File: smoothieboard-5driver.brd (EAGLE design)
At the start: 129.5 x 105.1 mm, 270 parts, among them IC1 LPC1769, IC10 LM1117-3.3V, IC11 78L12F, IC12 A4982, IC2 A4982, IC3 A4982, IC4 MCP44X1, IC5 A4982, IC6 A4982, IC9 MCP44X1, J10 POWER_JACKSMD, Q1 BSL207SP, Q2 12MHz, Q3 25MHz, Q4 ZXMN4A06, Q5 AOT240L, Q6 AOT240L, Q7 AOT240L, Q8 ZXMN4A06, Q9 ZXMN4A06, U1 USD-SOCKETNEW, X14 USBPTH

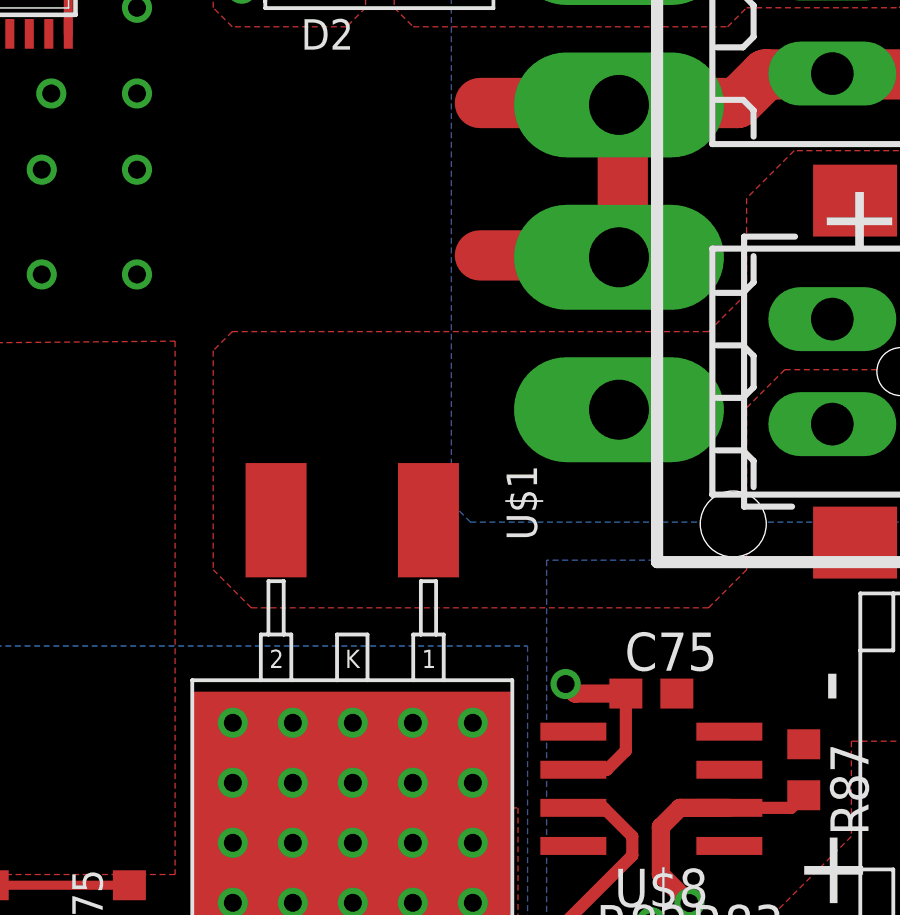
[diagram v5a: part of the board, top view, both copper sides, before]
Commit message: Change type of primary diode to a more robust type with lower Vf, add a helper diode to prevent damage from primary diode's higher reverse leakage
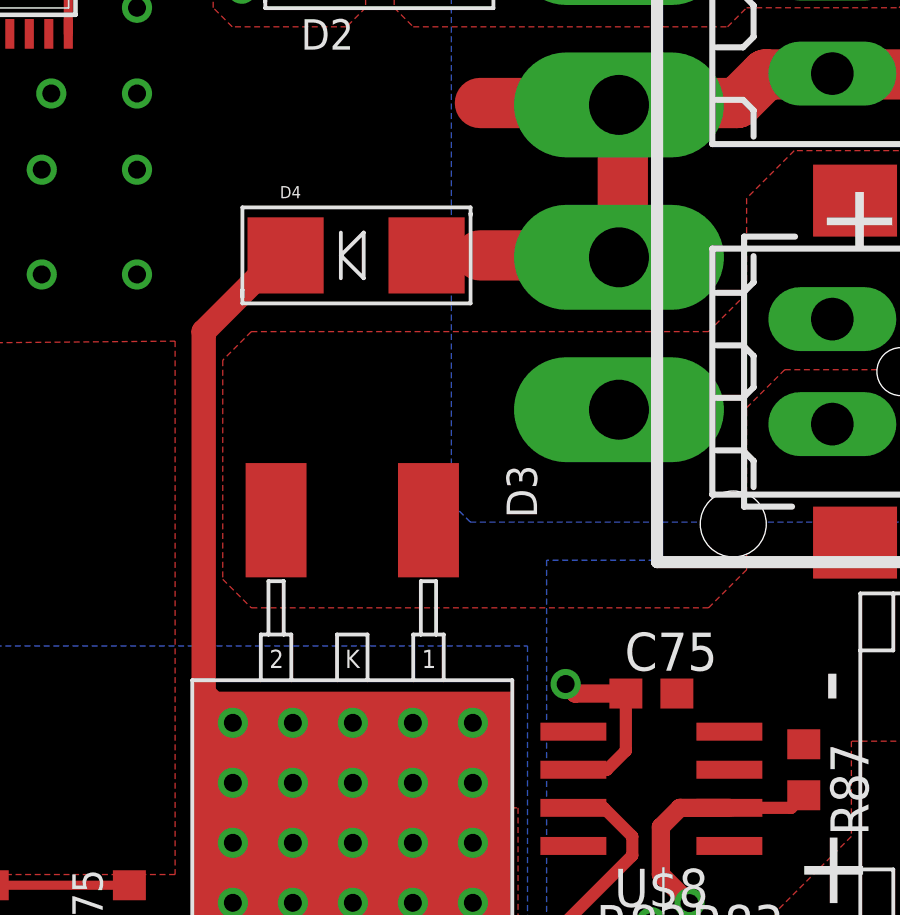
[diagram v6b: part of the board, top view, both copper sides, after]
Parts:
- added D4: MBRA210LT3, microbuilder:SMADIODE
- D3: value (none) -> VS-25CTQ045S
- renumbered U$1 to D3
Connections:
- net GND: now also D4.A
- net VBB: now also D4.C
- net VBB_IN: now also D3.1
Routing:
- net VBB: track 277.3 -> 294.5 mm
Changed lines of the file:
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@@
 <grid distance="12.5" unitdist="mil" unit="mil" style="dots" multiple="8" display="no" altdistance="6.25" altunitdist="mil" altunit="mil"/>
 <layers>
-<layer number="1" name="Top" color="4" fill="1" visible="no" active="yes"/>
+<layer number="1" name="Top" color="4" fill="1" visible="yes" active="yes"/>
 <layer number="2" name="Route2" color="2" fill="1" visible="no" active="yes"/>
 <layer number="3" name="Route3" color="4" fill="3" visible="no" active="no"/>
@@
 <layer number="13" name="Route13" color="4" fill="5" visible="no" active="no"/>
 <layer number="14" name="Route14" color="1" fill="6" visible="no" active="no"/>
-<layer number="15" name="Route15" color="5" fill="1" visible="yes" active="yes"/>
+<layer number="15" name="Route15" color="5" fill="1" visible="no" active="yes"/>
 <layer number="16" name="Bottom" color="1" fill="1" visible="no" active="yes"/>
 <layer number="17" name="Pads" color="2" fill="1" visible="yes" active="yes"/>
@@
 <attribute name="OC_FARNELL" value="unknown" x="109.0295" y="3.175" size="1.778" layer="27" display="off"/>
 </element>
-<element name="U$1" library="Geos" package="TO263AB" value="" x="108.7755" y="44.831" smashed="yes" rot="R180">
+<element name="D3" library="Geos" package="TO263AB" value="VS-25CTQ045S" x="108.7755" y="44.831" smashed="yes" rot="R180">
 <attribute name="NAME" x="107.569" y="44.1325" size="1.016" layer="25" rot="R270"/>
 <attribute name="VALUE" x="94.8055" y="35.941" size="1.27" layer="27" rot="R270"/>
@@
 <element name="U$9" library="eric_sorensen" package="1715250000" value="5MMCONN" x="124.46" y="31.75" rot="R90"/>
 <element name="R88" library="resistor" package="R0603" value="22R" x="120.65" y="17.78" rot="R180"/>
+<element name="D4" library="microbuilder" package="SMADIODE" value="MBRA210LT3" x="102.5525" y="51.1175"/>
 </elements>
 <signals>
@@
 <wire x1="109.22" y1="20.955" x2="109.22" y2="20.32" width="0.6096" layer="1"/>
 <wire x1="109.22" y1="20.32" x2="111.4425" y2="20.32" width="0.6096" layer="1"/>
+<contactref element="D4" pad="A"/>
 </signal>
 <signal name="3.3V">
@@
 <contactref element="R78" pad="2"/>
 <contactref element="C63" pad="+"/>
-<contactref element="U$1" pad="K"/>
+<contactref element="D3" pad="K"/>
 <contactref element="JP28" pad="2"/>
 <contactref element="JP11" pad="2"/>
@@
 <vertex x="57.785" y="17.145"/>
 </polygon>
+<contactref element="D4" pad="C"/>
+<wire x1="100.203" y1="51.1175" x2="100.0125" y2="51.1175" width="0.8128" layer="1"/>
+<wire x1="100.0125" y1="51.1175" x2="97.4725" y2="48.5775" width="0.8128" layer="1"/>
+<wire x1="97.4725" y1="48.5775" x2="97.4725" y2="36.51" width="0.8128" layer="1"/>
+<wire x1="97.4725" y1="36.51" x2="98.445" y2="35.5375" width="0.8128" layer="1"/>
 </signal>
 <signal name="P0W">
@@
 <contactref element="J10" pad="P$4"/>
 <contactref element="X11" pad="1"/>
-<contactref element="U$1" pad="2"/>
+<contactref element="D3" pad="2"/>
 <contactref element="POWER" pad="P$1"/>
 <polygon width="0.254" layer="1" thermals="no">
@@
 <vertex x="115.57" y="49.8475"/>
 <vertex x="114.3" y="48.5775"/>
-<vertex x="98.425" y="48.5775"/>
-<vertex x="97.79" y="47.9425"/>
-<vertex x="97.79" y="40.64"/>
+<vertex x="99.06" y="48.5775"/>
+<vertex x="98.1075" y="47.625"/>
+<vertex x="98.1075" y="40.3225"/>
 <vertex x="99.06" y="39.37"/>
 <vertex x="114.3" y="39.37"/>
@@
 <vertex x="117.1575" y="54.61"/>
 </polygon>
+<contactref element="D3" pad="1"/>
 </signal>
 <signal name="N$60">

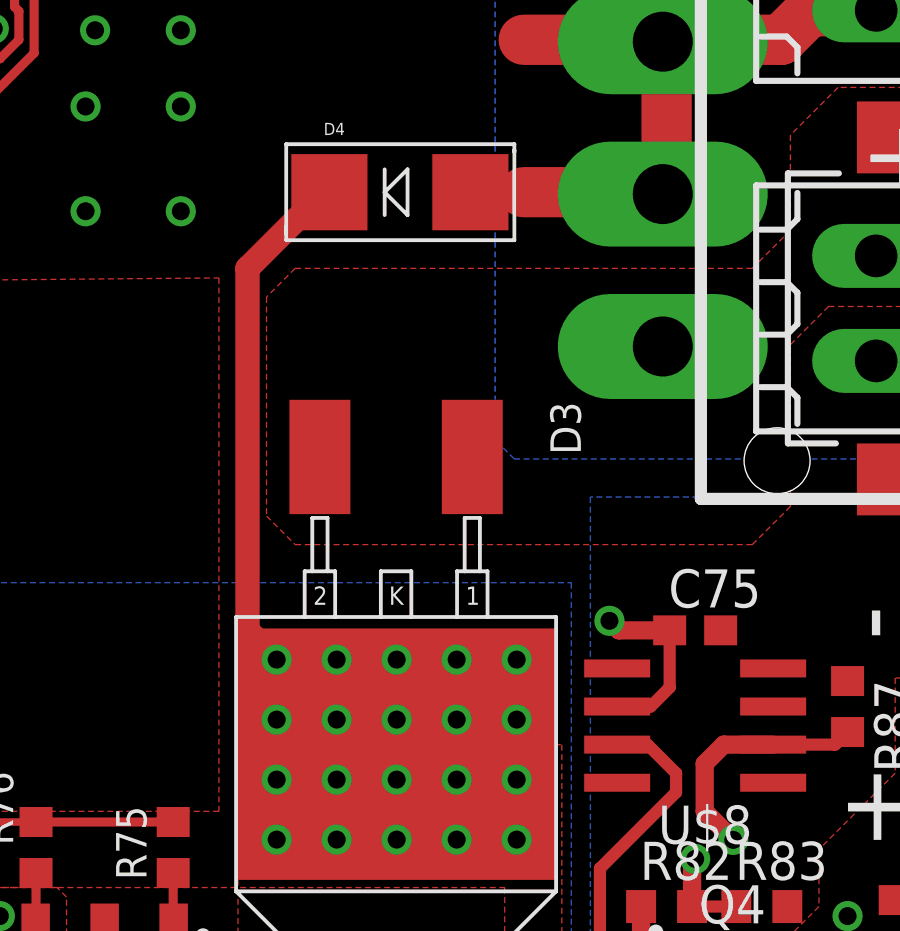
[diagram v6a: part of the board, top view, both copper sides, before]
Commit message: Alternative reverse polarity protection using a P-MOSFET. Do not populate both P-MOSFET and Diode footprints, the parts overlap
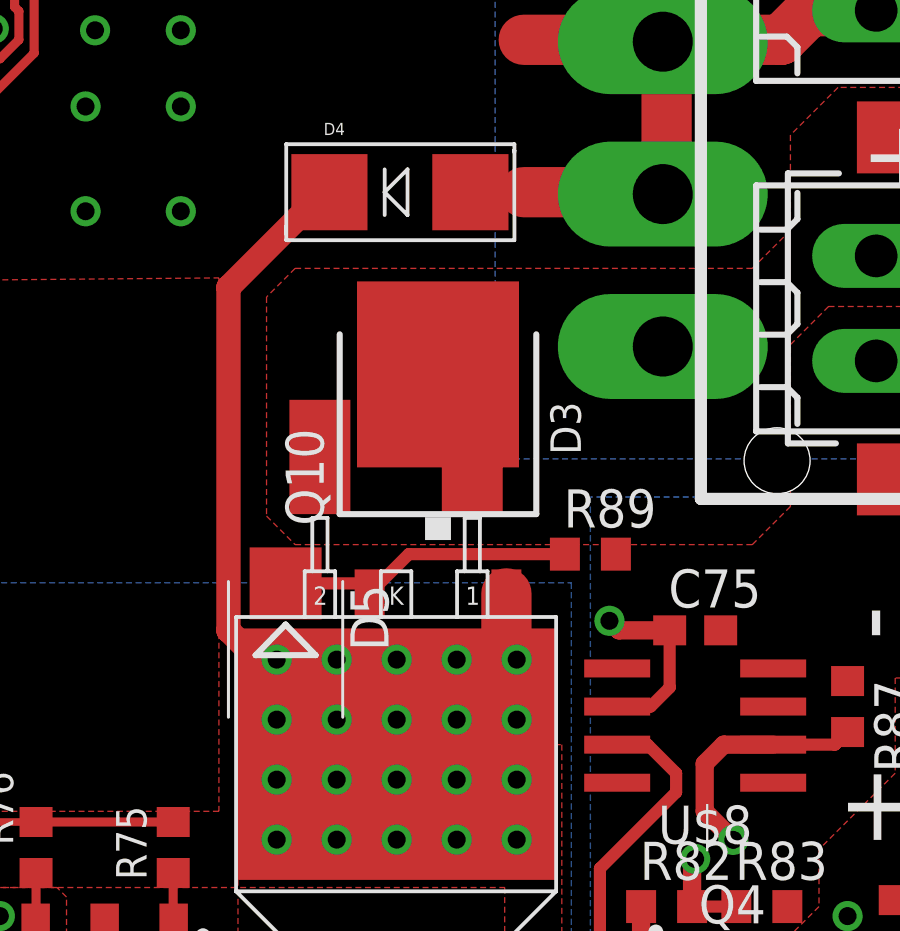
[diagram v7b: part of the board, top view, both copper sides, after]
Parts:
- added D5: 12v, diode:SMB
- added Q10: SUD50P04-08-GE3, transistor-fet:TO252
- added R89: 10k, resistor:R0603
- D4: value MBRA210LT3 -> B1100-13-F
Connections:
- new net N$111: D5.C, Q10.1, R89.1
- net GND: now also R89.2
- net VBB: now also D5.A, Q10.2
- net VBB_IN: now also Q10.3
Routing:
- net N$111: track 0.00 -> 9.99 mm
- net VBB: track 294.5 -> 297.7 mm
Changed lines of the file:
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@@
 <element name="U$9" library="eric_sorensen" package="1715250000" value="5MMCONN" x="124.46" y="31.75" rot="R90"/>
 <element name="R88" library="resistor" package="R0603" value="22R" x="120.65" y="17.78" rot="R180"/>
-<element name="D4" library="microbuilder" package="SMADIODE" value="MBRA210LT3" x="102.5525" y="51.1175"/>
+<element name="D4" library="microbuilder" package="SMADIODE" value="B1100-13-F" x="102.5525" y="51.1175"/>
+<element name="Q10" library="transistor-fet" package="TO252" value="SUD50P04-08-GE3" x="103.8225" y="42.545"/>
+<element name="R89" library="resistor" package="R0603" value="10k" x="108.9025" y="39.0525"/>
+<element name="D5" library="diode" package="SMB" value="12v" x="98.7425" y="35.8775" rot="R270"/>
 </elements>
 <signals>
@@
 <wire x1="109.22" y1="20.32" x2="111.4425" y2="20.32" width="0.6096" layer="1"/>
 <contactref element="D4" pad="A"/>
+<contactref element="R89" pad="2"/>
 </signal>
 <signal name="3.3V">
@@
 <contactref element="D4" pad="C"/>
 <wire x1="100.203" y1="51.1175" x2="100.0125" y2="51.1175" width="0.8128" layer="1"/>
-<wire x1="100.0125" y1="51.1175" x2="97.4725" y2="48.5775" width="0.8128" layer="1"/>
-<wire x1="97.4725" y1="48.5775" x2="97.4725" y2="36.51" width="0.8128" layer="1"/>
-<wire x1="97.4725" y1="36.51" x2="98.445" y2="35.5375" width="0.8128" layer="1"/>
+<wire x1="100.0125" y1="51.1175" x2="96.8375" y2="47.9425" width="0.8128" layer="1"/>
+<wire x1="96.8375" y1="47.9425" x2="96.8375" y2="36.51" width="0.8128" layer="1"/>
+<contactref element="Q10" pad="2"/>
+<contactref element="D5" pad="A"/>
+<wire x1="106.1025" y1="37.745" x2="106.1025" y2="35.88" width="1.6764" layer="1"/>
+<wire x1="106.1025" y1="35.88" x2="106.445" y2="35.5375" width="1.6764" layer="1"/>
+<wire x1="98.445" y1="35.5375" x2="97.81" y2="35.5375" width="0.8128" layer="1"/>
+<wire x1="97.81" y1="35.5375" x2="96.8375" y2="36.51" width="0.8128" layer="1"/>
 </signal>
 <signal name="P0W">
@@
 </polygon>
 <contactref element="D3" pad="1"/>
+<contactref element="Q10" pad="3"/>
 </signal>
 <signal name="N$60">
@@
 <wire x1="118.11" y1="17.78" x2="119.8" y2="17.78" width="0.4064" layer="1"/>
 </signal>
+<signal name="N$111">
+<contactref element="R89" pad="1"/>
+<contactref element="Q10" pad="1"/>
+<contactref element="D5" pad="C"/>
+<wire x1="108.0525" y1="39.0525" x2="102.85" y2="39.0525" width="0.4064" layer="1"/>
+<wire x1="102.85" y1="39.0525" x2="101.5425" y2="37.745" width="0.4064" layer="1"/>
+<wire x1="98.7425" y1="38.0775" x2="101.21" y2="38.0775" width="0.4064" layer="1"/>
+<wire x1="101.21" y1="38.0775" x2="101.5425" y2="37.745" width="0.4064" layer="1"/>
+</signal>
 </signals>

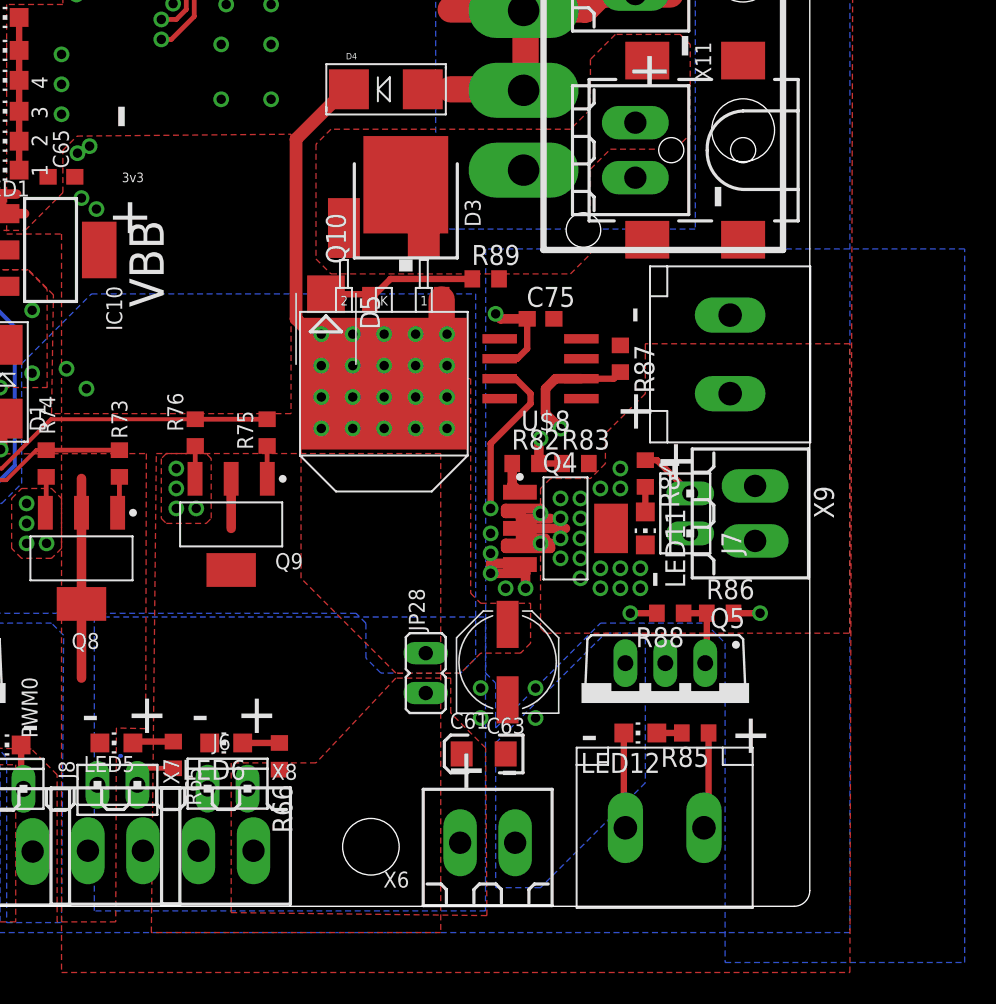
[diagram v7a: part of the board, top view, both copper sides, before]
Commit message: add some heatsinking for reverse polarity mosfet on back of board using thermal vias
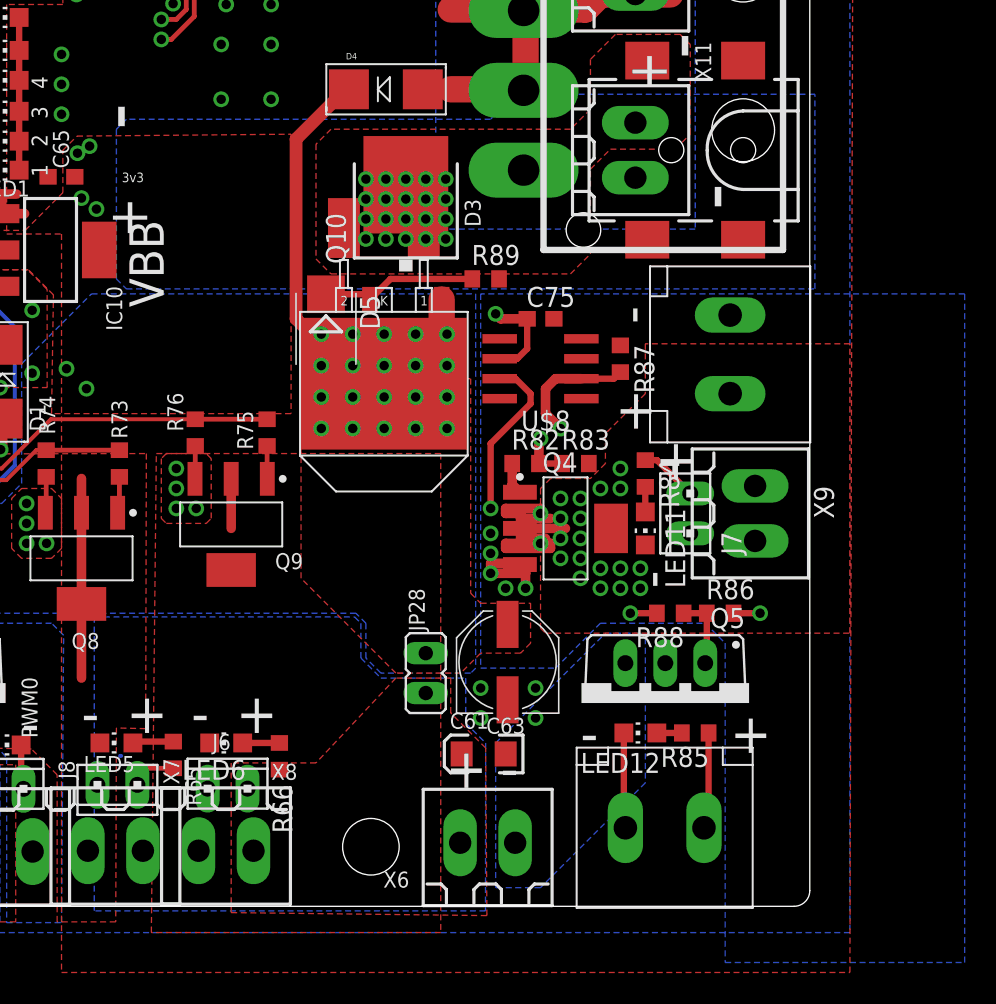
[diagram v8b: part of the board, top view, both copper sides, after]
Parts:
- D5: value 12v -> 15v
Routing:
- added copper zone on layer 16, net VBB_IN
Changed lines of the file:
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@@
 <grid distance="12.5" unitdist="mil" unit="mil" style="dots" multiple="8" display="no" altdistance="6.25" altunitdist="mil" altunit="mil"/>
 <layers>
-<layer number="1" name="Top" color="4" fill="1" visible="yes" active="yes"/>
+<layer number="1" name="Top" color="4" fill="1" visible="no" active="yes"/>
 <layer number="2" name="Route2" color="2" fill="1" visible="no" active="yes"/>
 <layer number="3" name="Route3" color="4" fill="3" visible="no" active="no"/>
@@
 <layer number="14" name="Route14" color="1" fill="6" visible="no" active="no"/>
 <layer number="15" name="Route15" color="5" fill="1" visible="no" active="yes"/>
-<layer number="16" name="Bottom" color="1" fill="1" visible="no" active="yes"/>
+<layer number="16" name="Bottom" color="1" fill="1" visible="yes" active="yes"/>
 <layer number="17" name="Pads" color="2" fill="1" visible="yes" active="yes"/>
 <layer number="18" name="Vias" color="2" fill="1" visible="yes" active="yes"/>
@@
 <element name="Q10" library="transistor-fet" package="TO252" value="SUD50P04-08-GE3" x="103.8225" y="42.545"/>
 <element name="R89" library="resistor" package="R0603" value="10k" x="108.9025" y="39.0525"/>
-<element name="D5" library="diode" package="SMB" value="12v" x="98.7425" y="35.8775" rot="R270"/>
+<element name="D5" library="diode" package="SMB" value="15v" x="98.7425" y="35.8775" rot="R270"/>
 </elements>
 <signals>
@@
 <vertex x="83.82" y="38.1"/>
 <vertex x="108.2675" y="38.1"/>
-<vertex x="108.2675" y="14.9225"/>
-<vertex x="107.315" y="13.97"/>
+<vertex x="108.2675" y="14.2875"/>
+<vertex x="107.95" y="13.97"/>
 <vertex x="102.235" y="13.97"/>
 <vertex x="101.2825" y="14.9225"/>
@@
 <contactref element="D3" pad="1"/>
 <contactref element="Q10" pad="3"/>
+<polygon width="0.254" layer="16" thermals="no" rank="4">
+<vertex x="86.0425" y="38.4175"/>
+<vertex x="129.8575" y="38.4175"/>
+<vertex x="129.8575" y="50.8"/>
+<vertex x="110.8075" y="50.8"/>
+<vertex x="109.22" y="49.2125"/>
+<vertex x="86.0425" y="49.2125"/>
+<vertex x="85.4075" y="48.5775"/>
+<vertex x="85.4075" y="39.0525"/>
+</polygon>
+<via x="101.2825" y="45.4025" extent="1-16" drill="0.6"/>
+<via x="102.5525" y="45.4025" extent="1-16" drill="0.6"/>
+<via x="103.8225" y="45.4025" extent="1-16" drill="0.6"/>
+<via x="105.0925" y="45.4025" extent="1-16" drill="0.6"/>
+<via x="106.3625" y="45.4025" extent="1-16" drill="0.6"/>
+<via x="106.3625" y="44.1325" extent="1-16" drill="0.6"/>
+<via x="105.0925" y="44.1325" extent="1-16" drill="0.6"/>
+<via x="103.8225" y="44.1325" extent="1-16" drill="0.6"/>
+<via x="102.5525" y="44.1325" extent="1-16" drill="0.6"/>
+<via x="101.2825" y="44.1325" extent="1-16" drill="0.6"/>
+<via x="101.2825" y="42.8625" extent="1-16" drill="0.6"/>
+<via x="102.5525" y="42.8625" extent="1-16" drill="0.6"/>
+<via x="103.8225" y="42.8625" extent="1-16" drill="0.6"/>
+<via x="105.0925" y="42.8625" extent="1-16" drill="0.6"/>
+<via x="106.3625" y="42.8625" extent="1-16" drill="0.6"/>
+<via x="106.3625" y="41.5925" extent="1-16" drill="0.6"/>
+<via x="105.0925" y="41.5925" extent="1-16" drill="0.6"/>
+<via x="103.8225" y="41.5925" extent="1-16" drill="0.6"/>
+<via x="102.5525" y="41.5925" extent="1-16" drill="0.6"/>
+<via x="101.2825" y="41.5925" extent="1-16" drill="0.6"/>
 </signal>
 <signal name="N$60">
@@
 <vertex x="106.68" y="11.43"/>
 </polygon>
-<polygon width="0.6096" layer="16" spacing="0.254" thermals="no" rank="4">
+<polygon width="0.254" layer="16" spacing="0.254" thermals="no" rank="4">
 <vertex x="84" y="-1.16"/>
 <vertex x="84" y="17.54"/>
-<vertex x="108.8925" y="17.54"/>
+<vertex x="100.57" y="17.54"/>
+<vertex x="100.965" y="17.145"/>
+<vertex x="100.965" y="14.9225"/>
+<vertex x="102.235" y="13.6525"/>
+<vertex x="107.6325" y="13.6525"/>
+<vertex x="107.6325" y="10.795"/>
+<vertex x="108.9025" y="9.525"/>
 <vertex x="108.8925" y="-1.16"/>
 </polygon>
@@
 <wire x1="111.4425" y1="22.5425" x2="112.7125" y2="22.5425" width="0.6096" layer="1"/>
 <polygon width="0.254" layer="16" thermals="no" rank="5">
-<vertex x="108.9025" y="40.9575"/>
-<vertex x="108.9025" y="13.97"/>
-<vertex x="109.5375" y="13.335"/>
-<vertex x="109.5375" y="10.4775"/>
+<vertex x="108.585" y="38.1"/>
+<vertex x="108.585" y="14.2875"/>
+<vertex x="113.3475" y="14.2875"/>
 <vertex x="116.205" y="17.145"/>
 <vertex x="122.8725" y="17.145"/>
@@
 <vertex x="124.1425" y="-4.445"/>
 <vertex x="139.3825" y="-4.445"/>
-<vertex x="139.3825" y="40.9575"/>
+<vertex x="139.3825" y="38.1"/>
 </polygon>
 <via x="116.205" y="20.6375" extent="1-16" drill="0.6"/>
